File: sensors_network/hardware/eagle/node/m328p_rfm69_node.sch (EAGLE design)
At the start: 32 parts, among them IC2 L6920, U1 M328P, U2 RFM69W, Y1 8MHz

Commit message: [sensors network] added missing ground connection for RFM69 module
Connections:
- net GND: now also U2.GND@1
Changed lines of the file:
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@@
 <setting verticaltext="up"/>
 </settings>
-<grid distance="0.01" unitdist="inch" unit="inch" style="dots" multiple="1" display="yes" altdistance="0.01" altunitdist="inch" altunit="inch"/>
+<grid distance="0.01" unitdist="inch" unit="inch" style="lines" multiple="1" display="no" altdistance="0.01" altunitdist="inch" altunit="inch"/>
 <layers>
 <layer number="1" name="Top" color="4" fill="1" visible="no" active="no"/>
@@
 <part name="+3V10" library="supply1" deviceset="+3V3" device=""/>
 <part name="+3V11" library="supply1" deviceset="+3V3" device=""/>
+<part name="GND23" library="supply1" deviceset="GND" device=""/>
 </parts>
 <sheets>
@@
 <instance part="+3V10" gate="G$1" x="96.266" y="61.214" rot="MR180"/>
 <instance part="+3V11" gate="G$1" x="121.666" y="60.706" rot="MR180"/>
+<instance part="GND23" gate="1" x="218.694" y="113.538"/>
 </instances>
 <busses>
@@
 <wire x1="128.27" y1="71.882" x2="122.682" y2="71.882" width="0.1524" layer="91"/>
 <pinref part="GND22" gate="1" pin="GND"/>
+</segment>
+<segment>
+<pinref part="U2" gate="G$1" pin="GND@1"/>
+<pinref part="GND23" gate="1" pin="GND"/>
+<wire x1="218.694" y1="116.078" x2="218.694" y2="117.856" width="0.1524" layer="91"/>
 </segment>
 </net>
@@
 </sheet>
 </sheets>
-<errors>
-</errors>
 </schematic>
 </drawing>

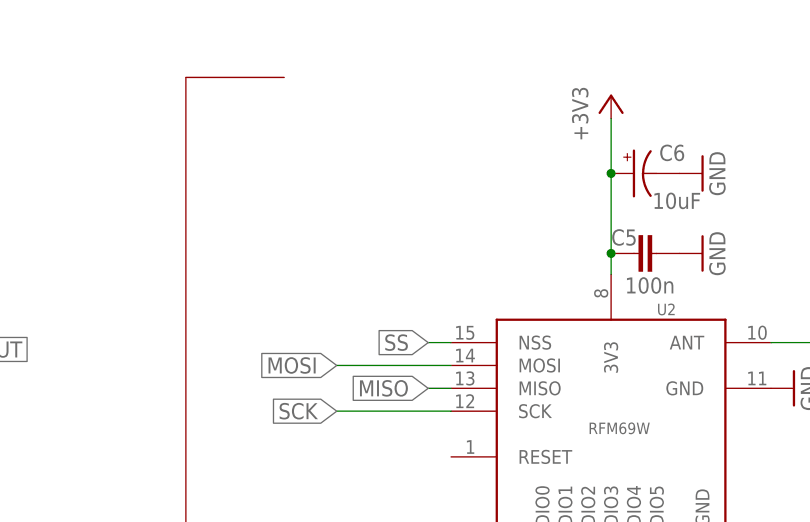
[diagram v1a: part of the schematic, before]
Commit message: [sensors_network] added 10K pull-up resistor for ICSP interference
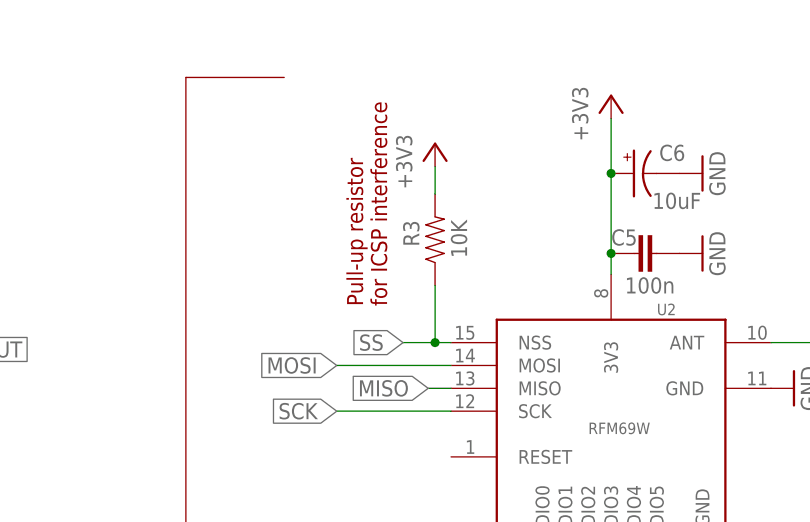
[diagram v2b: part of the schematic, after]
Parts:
- added R3: 10K, SparkFun-Resistors:RESISTOR0805-RES
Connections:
- net +3V3: now also R3.2
- net SS: now also R3.1
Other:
- note added: "Pull-up resistor for ICSP interference"
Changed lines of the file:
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@@
 <part name="+3V11" library="supply1" deviceset="+3V3" device=""/>
 <part name="GND23" library="supply1" deviceset="GND" device=""/>
+<part name="R3" library="SparkFun-Resistors" deviceset="RESISTOR" device="0805-RES" value="10K"/>
+<part name="+3V12" library="supply1" deviceset="+3V3" device=""/>
 </parts>
 <sheets>
@@
 <text x="216.662" y="29.464" size="1.778" layer="94">Voltage booster power supply</text>
 <text x="132.588" y="6.096" size="1.778" layer="94">AC energy measurement</text>
+<text x="183.642" y="149.86" size="1.778" layer="94" rot="R90">Pull-up resistor
+for ICSP interference</text>
 </plain>
 <instances>
@@
 <instance part="+3V11" gate="G$1" x="121.666" y="60.706" rot="MR180"/>
 <instance part="GND23" gate="1" x="218.694" y="113.538"/>
+<instance part="R3" gate="G$1" x="188.976" y="157.226" smashed="yes" rot="R90">
+<attribute name="NAME" x="187.2234" y="156.464" size="1.778" layer="95" rot="R90"/>
+<attribute name="VALUE" x="192.532" y="155.194" size="1.778" layer="96" rot="R90"/>
+</instance>
+<instance part="+3V12" gate="G$1" x="188.976" y="167.894"/>
 </instances>
 <busses>
@@
 <segment>
 <pinref part="U2" gate="G$1" pin="NSS"/>
-<wire x1="190.754" y1="145.796" x2="188.214" y2="145.796" width="0.1524" layer="91"/>
-<label x="188.214" y="145.796" size="1.778" layer="95" rot="R180" xref="yes"/>
+<wire x1="190.754" y1="145.796" x2="188.976" y2="145.796" width="0.1524" layer="91"/>
+<label x="185.42" y="145.796" size="1.778" layer="95" rot="R180" xref="yes"/>
+<pinref part="R3" gate="G$1" pin="1"/>
+<wire x1="188.976" y1="145.796" x2="185.42" y2="145.796" width="0.1524" layer="91"/>
+<wire x1="188.976" y1="152.146" x2="188.976" y2="145.796" width="0.1524" layer="91"/>
+<junction x="188.976" y="145.796"/>
 </segment>
 <segment>
@@
 <pinref part="+3V11" gate="G$1" pin="+3V3"/>
 </segment>
+<segment>
+<pinref part="R3" gate="G$1" pin="2"/>
+<pinref part="+3V12" gate="G$1" pin="+3V3"/>
+<wire x1="188.976" y1="165.354" x2="188.976" y2="162.306" width="0.1524" layer="91"/>
+</segment>
 </net>
 <net name="N$1" class="0">
@@
 </sheet>
 </sheets>
+<errors>
+</errors>
 </schematic>
 </drawing>
+<compatibility>
+<note version="6.3" minversion="6.2.2" severity="warning">
+Since Version 6.2.2 text objects can contain more than one line,
+which will not be processed correctly with this version.
+</note>
+</compatibility>
 </eagle>

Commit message: [sensors_network] pcb - added node id config switch and activity led
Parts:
- removed SJ1: V_BOOST1, jumper:SJ2W
- added D1: ACTIVITY, SparkFun-LED:LED0603
- added JP7: Ammeter probe, pinhead:PINHD-1X2
- added R5: 680, SparkFun-Passives:RESISTOR0805-RES
- added SW2: Node ID, SparkFun-Electromechanical:SW_DIP-8-SMT-HALFSIZE
- SJ2: value V_BOOST2 -> VB_EN_DIS
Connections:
- removed net A0: JP4.3, U1.PC0(ADC0)
- removed net A1: JP4.4, U1.PC1(ADC1)
- removed net N$7: C1.1, C9.+, IC2.!SHDN, IC2.FB, IC2.OUT, SJ2.1
- new net A6: JP4.3, U1.ADC6
- new net A7: JP4.4, U1.ADC7
- new net C0: SW2.2, U1.PC0(ADC0)
- new net C1: SW2.1, U1.PC1(ADC1)
- new net C2: SW2.3, U1.PD5(T1)
- new net C3: SW2.4, U1.PD6(AIN0)
- new net C4: SW2.5, U1.PD7(AIN1)
- new net C5: SW2.6, U1.PB0(ICP)
- new net C6: SW2.7, U1.PB1(OC1A)
- new net N$5: BAT3.+, JP7.2
- net +3V3: now also C1.1, C9.+, IC2.!SHDN, IC2.FB, IC2.OUT, SJ2.1; no longer SJ1.1, SJ2.2
- net BATT_LVL: now also C8.+, JP7.1, L1.2, SJ2.2; no longer BAT3.+, SJ1.2
- net D5: now also R5.1
- net GND: now also D1.C, SW2.10, SW2.11, SW2.12, SW2.13, SW2.14, SW2.15, SW2.16, SW2.9
- net N$2: now also D1.A, R5.2; no longer C8.+, L1.2, SJ1.3
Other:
- note added: "Node ID configuration switch"
- note added: "Node activity LED"
- moved on the sheet: BAT3, BAT4, JP2, JP4, JP5, JP6, SJ2
